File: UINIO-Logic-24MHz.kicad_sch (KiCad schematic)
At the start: 45 parts, among them J1 Conn_01x10_Male, U1 AT24CS64-XHM, U2 74HC245C, U3 ME6211C33M5G-N, U4 CY7C68013A-56LTX, Y1 24MHz

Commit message: Release UINIO-Logic-24MHz version 3.0.0.
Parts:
- D1: value Red LED -> LED Red
- D2: value Blue LED -> LED Yellow
- D3: value Blue LED -> LED Green
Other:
- moved on the sheet: R10, R11, R12, R13, R14, R15, R16, R9

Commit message: Prepare version 3.1.0.
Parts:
- removed J1: Conn_01x10_Male, Connector_PinHeader_2.54mm:PinHeader_1x10_P2.54mm_Vertical, symbol Connector:Conn_01x10_Male
- added J1: Conn_01x10_Pin, Connector_PinHeader_2.54mm:PinHeader_1x10_P2.54mm_Vertical, symbol Connector:Conn_01x10_Pin
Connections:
- net GND: now also J1.1 (Pin_1), J1.10 (Pin_10)
- net at R4.2: now also J1.6 (Pin_6)
- net at R2.2: now also J1.8 (Pin_8)
- net at R5.2: now also J1.5 (Pin_5)
- net at R3.2: now also J1.7 (Pin_7)
- net at R6.2: now also J1.4 (Pin_4)
- net at R8.2: now also J1.2 (Pin_2)
- net at R7.2: now also J1.3 (Pin_3)
- net at R1.2: now also J1.9 (Pin_9)

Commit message: Release UINIO-Logic-24MHz version 3.1.0.
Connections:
- net at R25.1: now also USB1.B5 (CC2); no longer USB1.A8 (SBU1)
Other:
- moved on the sheet: R25
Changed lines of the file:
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@@
   (no_connect (at 203.2 68.58))
   (no_connect (at 53.34 165.1))
-  (no_connect (at 53.34 157.48))
+  (no_connect (at 54.61 149.86))
   (no_connect (at 203.2 93.98))
   (no_connect (at 203.2 109.22))
@@
     (stroke (width 0) (type default))
   )
+  (wire (pts (xy 53.34 157.48) (xy 84.455 157.48))
+    (stroke (width 0) (type default))
+  )
   (wire (pts (xy 269.24 71.12) (xy 238.76 71.12))
     (stroke (width 0) (type default))
@@
     (stroke (width 0) (type default))
   )
-  (wire (pts (xy 62.23 142.24) (xy 64.77 142.24))
+  (wire (pts (xy 62.23 142.24) (xy 65.405 142.24))
     (stroke (width 0) (type default))
   )
@@
     (stroke (width 0) (type default))
   )
-  (wire (pts (xy 62.23 149.86) (xy 64.77 149.86))
+  (wire (pts (xy 84.455 165.735) (xy 84.455 168.275))
     (stroke (width 0) (type default))
   )
@@
   )
   (wire (pts (xy 66.04 34.29) (xy 71.12 34.29))
+    (stroke (width 0) (type default))
+  )
+  (wire (pts (xy 84.455 157.48) (xy 84.455 158.115))
     (stroke (width 0) (type default))
   )
@@
     )
   )
-  (symbol (lib_id "power:GND") (at 64.77 149.86 90) (unit 1)
-    (in_bom yes) (on_board yes) (dnp no)
-    (property "Reference" "#PWR033" (at 71.12 149.86 0)
-      (effects (font (size 1.27 1.27)) hide)
-    )
-    (property "Value" "GND" (at 69.85 149.86 90)
-      (effects (font (size 1.27 1.27)))
-    )
-    (property "Footprint" "" (at 64.77 149.86 0)
-      (effects (font (size 1.27 1.27)) hide)
-    )
-    (property "Datasheet" "" (at 64.77 149.86 0)
+  (symbol (lib_id "power:GND") (at 84.455 168.275 0) (unit 1)
+    (in_bom yes) (on_board yes) (dnp no)
+    (property "Reference" "#PWR033" (at 84.455 174.625 0)
+      (effects (font (size 1.27 1.27)) hide)
+    )
+    (property "Value" "GND" (at 84.455 172.085 0)
+      (effects (font (size 1.27 1.27)))
+    )
+    (property "Footprint" "" (at 84.455 168.275 0)
+      (effects (font (size 1.27 1.27)) hide)
+    )
+    (property "Datasheet" "" (at 84.455 168.275 0)
       (effects (font (size 1.27 1.27)) hide)
     )
@@
     )
   )
-  (symbol (lib_id "power:GND") (at 64.77 142.24 90) (unit 1)
-    (in_bom yes) (on_board yes) (dnp no)
-    (property "Reference" "#PWR032" (at 71.12 142.24 0)
-      (effects (font (size 1.27 1.27)) hide)
-    )
-    (property "Value" "GND" (at 69.85 142.24 90)
-      (effects (font (size 1.27 1.27)))
-    )
-    (property "Footprint" "" (at 64.77 142.24 0)
-      (effects (font (size 1.27 1.27)) hide)
-    )
-    (property "Datasheet" "" (at 64.77 142.24 0)
+  (symbol (lib_id "power:GND") (at 65.405 142.24 90) (unit 1)
+    (in_bom yes) (on_board yes) (dnp no)
+    (property "Reference" "#PWR032" (at 71.755 142.24 0)
+      (effects (font (size 1.27 1.27)) hide)
+    )
+    (property "Value" "GND" (at 70.485 142.24 90)
+      (effects (font (size 1.27 1.27)))
+    )
+    (property "Footprint" "" (at 65.405 142.24 0)
+      (effects (font (size 1.27 1.27)) hide)
+    )
+    (property "Datasheet" "" (at 65.405 142.24 0)
       (effects (font (size 1.27 1.27)) hide)
     )
@@
     )
   )
-  (symbol (lib_id "Device:R") (at 58.42 149.86 90) (unit 1)
-    (in_bom yes) (on_board yes) (dnp no)
-    (property "Reference" "R25" (at 64.77 151.13 90)
-      (effects (font (size 1.27 1.27)) (justify left))
-    )
-    (property "Value" "5.1K" (at 60.325 149.86 90)
-      (effects (font (size 1.27 1.27)) (justify left))
-    )
-    (property "Footprint" "Resistor_SMD:R_0402_1005Metric" (at 58.42 151.638 90)
-      (effects (font (size 1.27 1.27)) hide)
-    )
-    (property "Datasheet" "~" (at 58.42 149.86 0)
+  (symbol (lib_id "Device:R") (at 84.455 161.925 0) (unit 1)
+    (in_bom yes) (on_board yes) (dnp no)
+    (property "Reference" "R25" (at 86.995 163.83 90)
+      (effects (font (size 1.27 1.27)) (justify left))
+    )
+    (property "Value" "5.1K" (at 84.455 163.83 90)
+      (effects (font (size 1.27 1.27)) (justify left))
+    )
+    (property "Footprint" "Resistor_SMD:R_0402_1005Metric" (at 82.677 161.925 90)
+      (effects (font (size 1.27 1.27)) hide)
+    )
+    (property "Datasheet" "~" (at 84.455 161.925 0)
       (effects (font (size 1.27 1.27)) hide)
     )
@@
   (symbol (lib_id "Device:R") (at 58.42 142.24 90) (unit 1)
     (in_bom yes) (on_board yes) (dnp no)
-    (property "Reference" "R24" (at 64.77 143.51 90)
-      (effects (font (size 1.27 1.27)) (justify left))
-    )
+    (property "Reference" "R24" (at 65.405 143.51 90)
+      (effects (font (size 1.27 1.27)) (justify left))
+    )

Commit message: Release UINIO-Logic-24MHz version 3.1.1.
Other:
- company: 电子技术博客 UinIO.com -> UinIO.com 电子技术实验室
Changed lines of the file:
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@@
   (title_block
     (title "UINIO-Logic-24MHz")
-    (date "2023-06-29")
-    (rev "Version 3.1.0")
-    (company "电子技术博客 UinIO.com")
+    (date "2024-01-11")
+    (rev "Version 3.1.1")
+    (company "UinIO.com 电子技术实验室")
   )
   (junction (at 193.04 93.98) (diameter 0) (color 0 0 0 0)

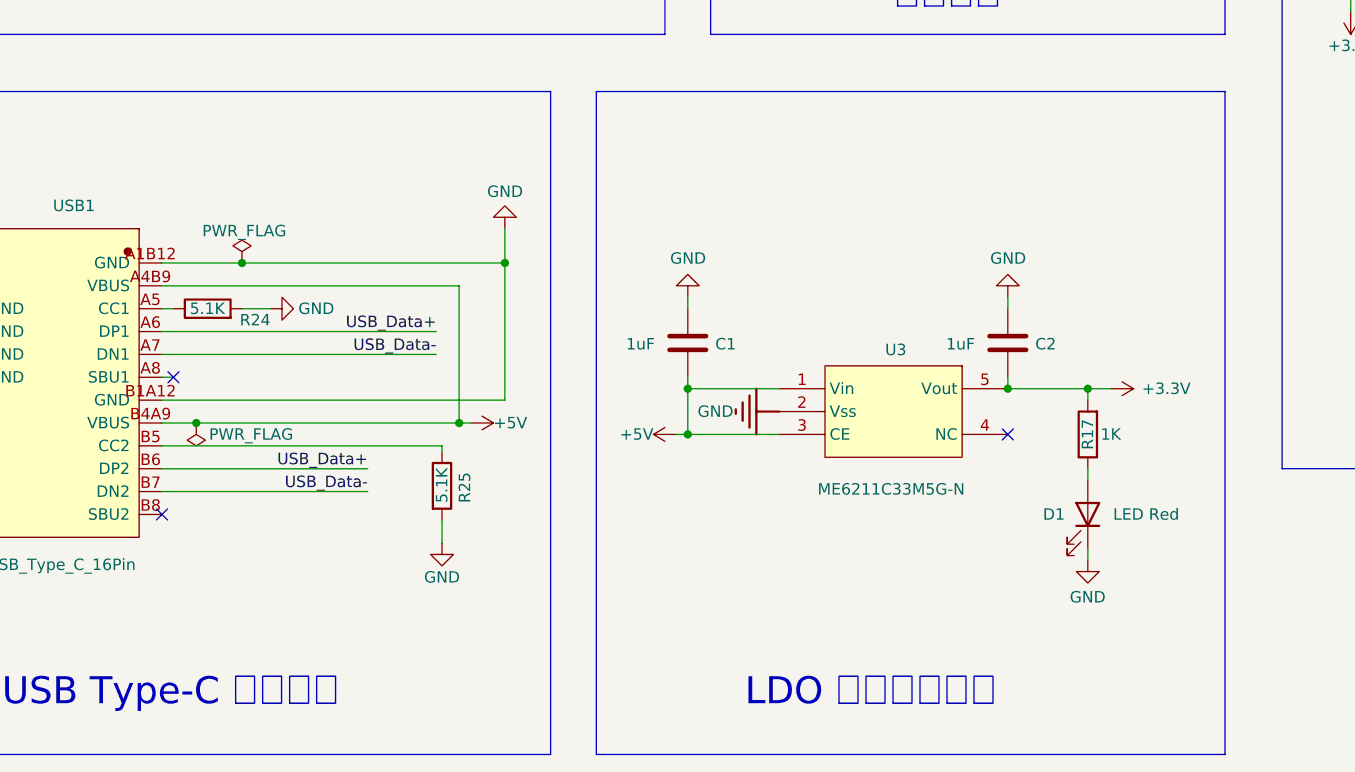
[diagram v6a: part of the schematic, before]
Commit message: Reorganize component.
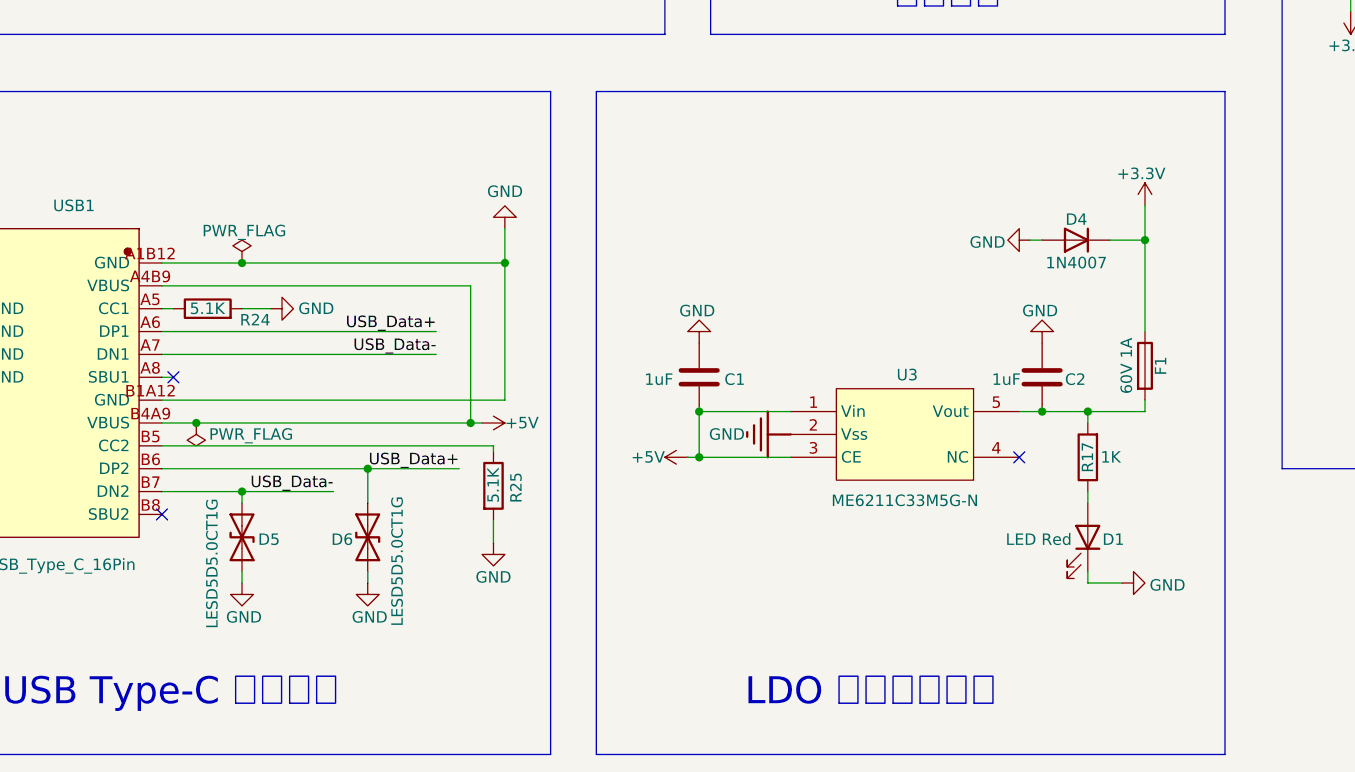
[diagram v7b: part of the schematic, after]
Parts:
- added D4: 1N4007, Diode_SMD:D_SMA, symbol Diode:1N4007
- added D5, D6: LESD5D5.0CT1G, Diode_SMD:D_SOD-523, symbol Diode:1N630xCA
- added F1: 60V 1A, Fuse:Fuse_1206_3216Metric, symbol Device:Fuse
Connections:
- net +3.3V: now also D4.1 (K), F1.1; no longer C2.2, R17.2, U3.5 (Vout)
- net GND: now also D4.2 (A), D5.1 (A1), D6.1 (A1)
- net USB_Data+: now also D6.2 (A2)
- net USB_Data-: now also D5.2 (A2)
- new net: C2.2, F1.2, R17.2, U3.5 (Vout)
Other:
- moved on the sheet: C1, C2, D1, R17, R25, U3

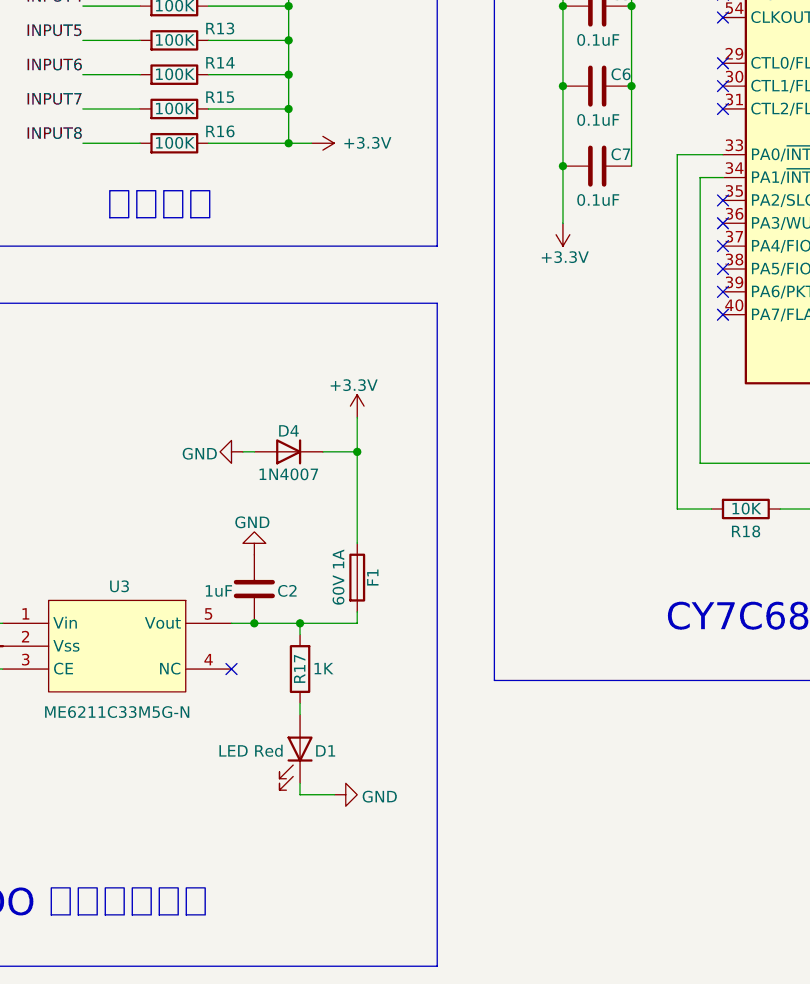
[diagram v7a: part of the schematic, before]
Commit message: Reorganize component.
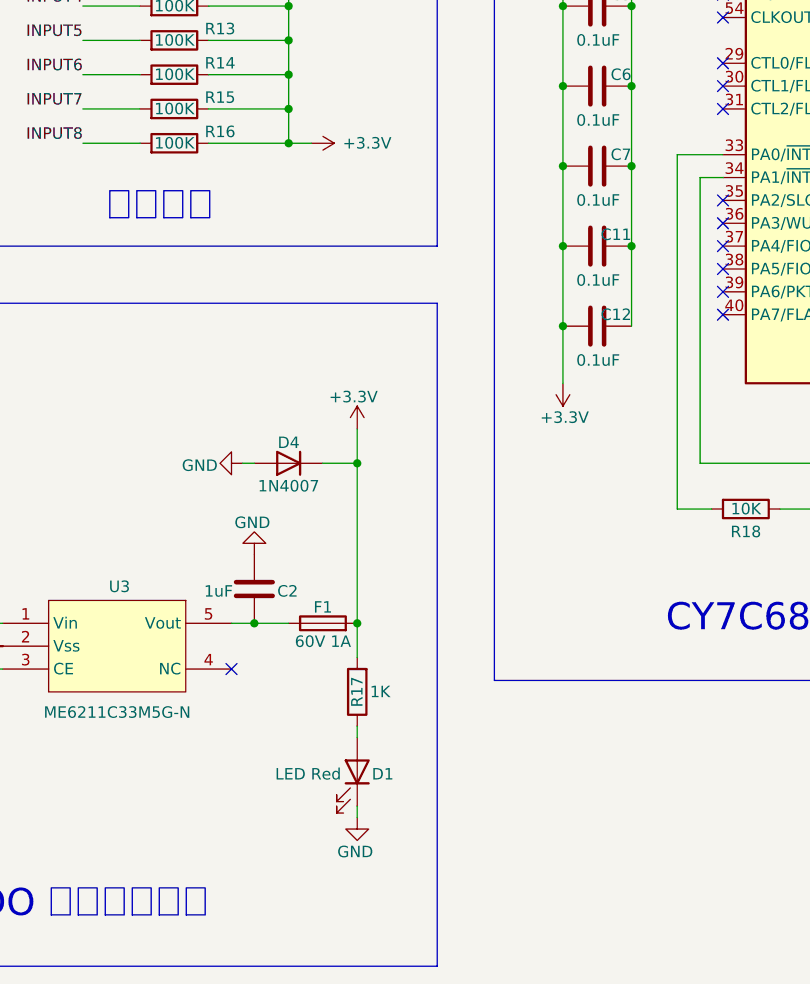
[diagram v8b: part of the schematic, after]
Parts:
- added C11, C12: 0.1uF, Capacitor_SMD:C_0402_1005Metric, symbol Device:C
- R17, R24, R25: footprint Resistor_SMD:R_0402_1005Metric -> Resistor_SMD:R_0603_1608Metric
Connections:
- net +3.3V: now also F1.2, R17.2, C11.1, C12.1; no longer F1.1
- net GND: now also C11.2, C12.2
- net at C2.2, U3.5 (Vout): now also F1.1; no longer F1.2, R17.2
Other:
- moved on the sheet: D1, D4, F1, R17
